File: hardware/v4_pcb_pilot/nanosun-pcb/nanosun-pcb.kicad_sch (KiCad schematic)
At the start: 30 parts, among them J1 +12V, J2 DIN, J3 GND

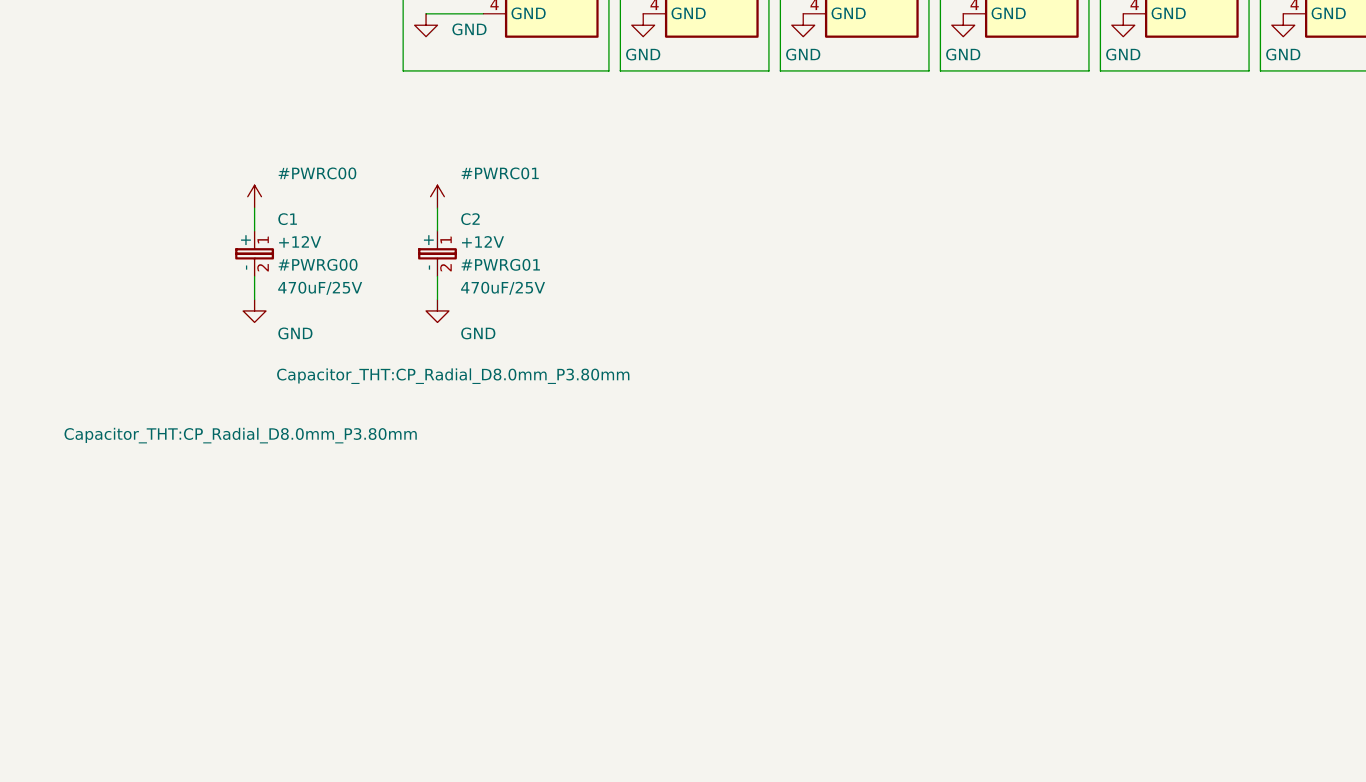
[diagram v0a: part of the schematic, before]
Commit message: Add MP1584EN buck regulator mounting and remove stray silkscreen rect
Adds a 12V->5V power path on the back side of the PCB:
- New MP1584EN_Module footprint (22x17 mm body, four 3x5 mm corner SMD
  pads on B.Cu) for the generic adjustable buck breakout.
- New schematic symbol with VIN/GND/GND/+5V pins, plus a +5V WireSolderPad
  (J4) so the regulated rail can be tapped off-board. Uses a new local
  power:+5V net driven by the regulator's power_out pin.
- Removes a leftover B.SilkS rectangle that was no longer needed.

ERC: 0 violations.

Co-Authored-By: Claude Opus 4.6 <noreply@anthropic.com>
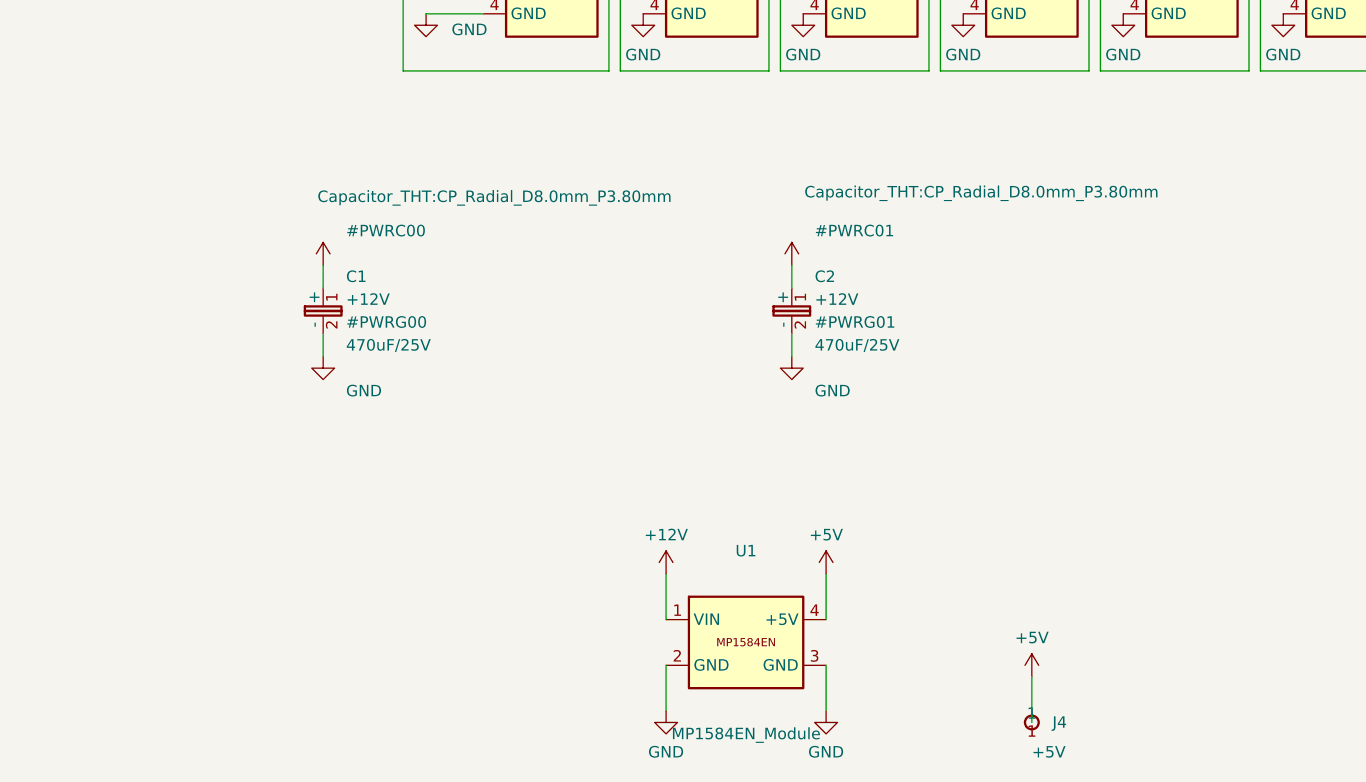
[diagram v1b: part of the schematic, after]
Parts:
- added J4: +5V, nanosun-pcb:WireSolderPad_1, symbol nanosun-pcb:WireSolderPad
- added U1: MP1584EN_Module, nanosun-pcb:MP1584EN_Module, symbol nanosun-pcb:MP1584EN_Module
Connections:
- net +12V: now also U1.1 (VIN)
- net GND: now also U1.2 (GND), U1.3 (GND)
- new net +5V: J4.1, U1.4 (+5V)
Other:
- moved on the sheet: C1, C2
